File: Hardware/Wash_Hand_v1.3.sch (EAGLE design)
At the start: 62 parts, among them IC1 LM358D, IC2 LP298XS, IC3 405016TSSOP, J1 I2C, J2 ICSP, J3 SPI, J4 9V_CONN, J5 EXT_VCC, J6 6_PIN_SERIAL_CABLEPTH, Q1 16.0 Mhz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

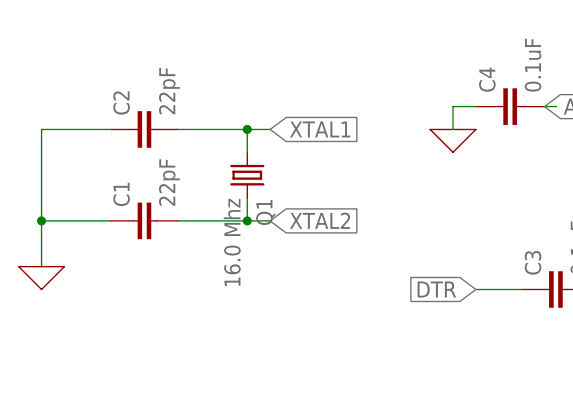
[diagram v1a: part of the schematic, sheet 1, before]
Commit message: Board/Schematic: Change 22pf to 10pf
Which makes the crystal work..

Signed-off-by: Konrad Rzeszutek Wilk <konrad@kernel.org>
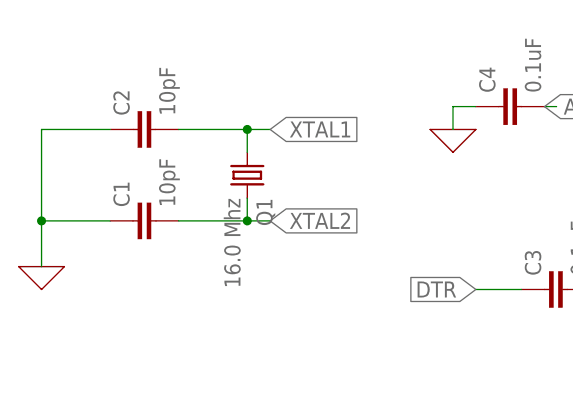
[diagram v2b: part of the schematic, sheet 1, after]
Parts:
- C1, C2: value 22pF -> 10pF
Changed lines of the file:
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@@
 <parts>
 <part name="Q1" library="adafruit" library_urn="urn:adsk.eagle:library:420" deviceset="CRYSTAL" device="HC49S" package3d_urn="urn:adsk.eagle:package:6240901/1" value="16.0 Mhz"/>
-<part name="C1" library="SparkFun-Capacitors" library_urn="urn:adsk.eagle:library:510" deviceset="10UF" device="-1206-6.3V-20%" package3d_urn="urn:adsk.eagle:package:37426/1" value="22pF"/>
-<part name="C2" library="SparkFun-Capacitors" library_urn="urn:adsk.eagle:library:510" deviceset="10UF" device="-1206-6.3V-20%" package3d_urn="urn:adsk.eagle:package:37426/1" value="22pF"/>
+<part name="C1" library="SparkFun-Capacitors" library_urn="urn:adsk.eagle:library:510" deviceset="10UF" device="-1206-6.3V-20%" package3d_urn="urn:adsk.eagle:package:37426/1" value="10pF"/>
+<part name="C2" library="SparkFun-Capacitors" library_urn="urn:adsk.eagle:library:510" deviceset="10UF" device="-1206-6.3V-20%" package3d_urn="urn:adsk.eagle:package:37426/1" value="10pF"/>
 <part name="X_2" library="ngspice-simulation" library_urn="urn:adsk.eagle:library:527439" deviceset="GND" device=""/>
 <part name="U$4" library="darnok_usb" deviceset="USB_MICROB_10118194_AMPHENOL" device="" package3d_urn="urn:adsk.eagle:package:21769933/1"/>

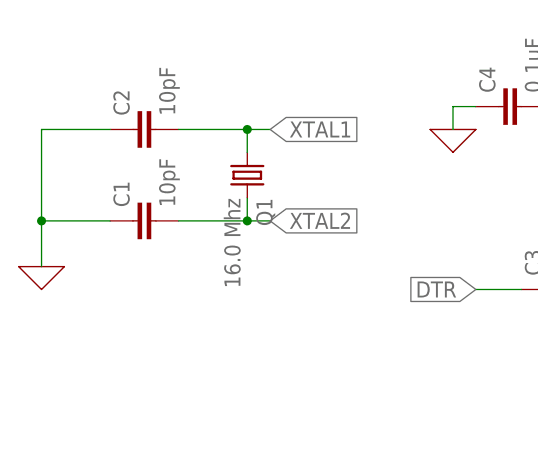
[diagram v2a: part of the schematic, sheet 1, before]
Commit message: Board/Schematic: Fix the 16MHz/10pF capacitors.
The way they are were in the schematic looked right.
Two capacitors off the crystal. Both capacitors go to
ground. Except that what Eagle decided it should be was:

XTAL1         XTAL2
|             |
+--[CRYSTAL]--+
             [CAP]
              |
             [CAP]
              |
             [GND]

Instead of the:

XTAL1         XTAL2
|             |
+--[CRYSTAL]--+
[CAP]        [CAP]
|             |
\------+------/
     [GND]

This fixes it.

Signed-off-by: Konrad Rzeszutek Wilk <konrad@kernel.org>
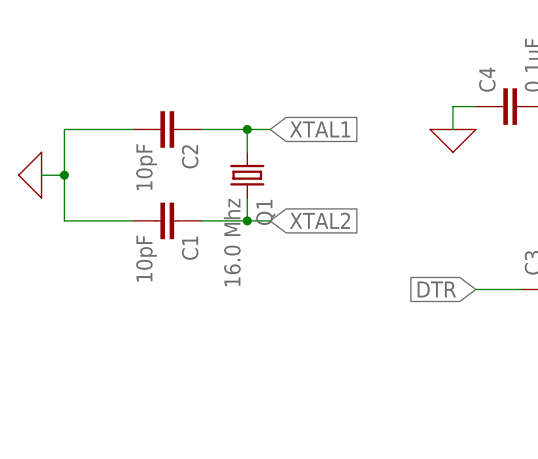
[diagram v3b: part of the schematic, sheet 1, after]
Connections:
- net 0: now also C1.2, C2.2; no longer C1.1, C2.1
- net XTAL1: now also C2.1; no longer C2.2
- net XTAL2: now also C1.1; no longer C1.2
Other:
- moved on the sheet: C1, C2
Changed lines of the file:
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@@
 <attribute name="VALUE" x="30.48" y="185.42" size="1.778" layer="96" rot="R270"/>
 </instance>
-<instance part="C1" gate="G$1" x="22.86" y="182.88" smashed="yes" rot="R90">
-<attribute name="NAME" x="19.939" y="184.404" size="1.778" layer="95" font="vector" rot="R90"/>
-<attribute name="VALUE" x="25.019" y="184.404" size="1.778" layer="96" font="vector" rot="R90"/>
-</instance>
-<instance part="C2" gate="G$1" x="22.86" y="193.04" smashed="yes" rot="R90">
-<attribute name="NAME" x="19.939" y="194.564" size="1.778" layer="95" font="vector" rot="R90"/>
-<attribute name="VALUE" x="25.019" y="194.564" size="1.778" layer="96" font="vector" rot="R90"/>
+<instance part="C1" gate="G$1" x="22.86" y="182.88" smashed="yes" rot="R270">
+<attribute name="NAME" x="25.781" y="181.356" size="1.778" layer="95" font="vector" rot="R270"/>
+<attribute name="VALUE" x="20.701" y="181.356" size="1.778" layer="96" font="vector" rot="R270"/>
+</instance>
+<instance part="C2" gate="G$1" x="22.86" y="193.04" smashed="yes" rot="R270">
+<attribute name="NAME" x="25.781" y="191.516" size="1.778" layer="95" font="vector" rot="R270"/>
+<attribute name="VALUE" x="20.701" y="191.516" size="1.778" layer="96" font="vector" rot="R270"/>
 </instance>
 <instance part="U$5" gate="G$1" x="210.82" y="76.2" smashed="yes">
@@
 <attribute name="VALUE" x="93.98" y="180.34" size="1.27" layer="96" rot="R90"/>
 </instance>
-<instance part="X_3" gate="G$1" x="10.16" y="177.8" smashed="yes"/>
+<instance part="X_3" gate="G$1" x="10.16" y="187.96" smashed="yes" rot="R270"/>
 <instance part="J1" gate="G$1" x="154.94" y="198.12" smashed="yes" rot="R180">
 <attribute name="VALUE" x="157.48" y="202.946" size="1.778" layer="96" font="vector" rot="R180"/>
@@
 <net name="0" class="0">
 <segment>
-<pinref part="X_3" gate="G$1" pin="0"/>
-<pinref part="C1" gate="G$1" pin="1"/>
-<wire x1="10.16" y1="193.04" x2="10.16" y2="182.88" width="0.1524" layer="91"/>
-<pinref part="C2" gate="G$1" pin="1"/>
-<wire x1="17.78" y1="193.04" x2="10.16" y2="193.04" width="0.1524" layer="91"/>
-<wire x1="17.78" y1="182.88" x2="10.16" y2="182.88" width="0.1524" layer="91"/>
-<junction x="10.16" y="182.88"/>
-<wire x1="10.16" y1="182.88" x2="10.16" y2="177.8" width="0.1524" layer="91"/>
-</segment>
-<segment>
 <pinref part="J5" gate="G$1" pin="1"/>
 <wire x1="38.1" y1="38.1" x2="45.72" y2="38.1" width="0.1524" layer="91"/>
@@
 <junction x="134.62" y="104.14"/>
 </segment>
+<segment>
+<pinref part="X_3" gate="G$1" pin="0"/>
+<wire x1="10.16" y1="187.96" x2="12.7" y2="187.96" width="0.1524" layer="91"/>
+<junction x="12.7" y="187.96"/>
+<wire x1="12.7" y1="187.96" x2="12.7" y2="193.04" width="0.1524" layer="91"/>
+<pinref part="C2" gate="G$1" pin="2"/>
+<wire x1="12.7" y1="193.04" x2="20.32" y2="193.04" width="0.1524" layer="91"/>
+<pinref part="C1" gate="G$1" pin="2"/>
+<wire x1="20.32" y1="182.88" x2="12.7" y2="182.88" width="0.1524" layer="91"/>
+<wire x1="12.7" y1="182.88" x2="12.7" y2="187.96" width="0.1524" layer="91"/>
+</segment>
 </net>
 <net name="D0" class="0">
@@
 <net name="XTAL2" class="0">
 <segment>
-<pinref part="C1" gate="G$1" pin="2"/>
 <pinref part="Q1" gate="G$1" pin="2"/>
-<wire x1="25.4" y1="182.88" x2="33.02" y2="182.88" width="0.1524" layer="91"/>
 <wire x1="33.02" y1="182.88" x2="33.02" y2="185.42" width="0.1524" layer="91"/>
 <wire x1="33.02" y1="182.88" x2="35.56" y2="182.88" width="0.1524" layer="91"/>
+<label x="35.56" y="182.88" size="1.778" layer="95" xref="yes"/>
+<pinref part="C1" gate="G$1" pin="1"/>
+<wire x1="27.94" y1="182.88" x2="33.02" y2="182.88" width="0.1524" layer="91"/>
 <junction x="33.02" y="182.88"/>
-<label x="35.56" y="182.88" size="1.778" layer="95" xref="yes"/>
 </segment>
 <segment>
@@
 <segment>
 <pinref part="Q1" gate="G$1" pin="1"/>
-<pinref part="C2" gate="G$1" pin="2"/>
-<wire x1="25.4" y1="193.04" x2="33.02" y2="193.04" width="0.1524" layer="91"/>
 <wire x1="33.02" y1="193.04" x2="33.02" y2="190.5" width="0.1524" layer="91"/>
 <wire x1="33.02" y1="193.04" x2="35.56" y2="193.04" width="0.1524" layer="91"/>
+<label x="35.56" y="193.04" size="1.778" layer="95" xref="yes"/>
 <junction x="33.02" y="193.04"/>
-<label x="35.56" y="193.04" size="1.778" layer="95" xref="yes"/>
-</segment>
-<segment>
+<pinref part="C2" gate="G$1" pin="1"/>
+<wire x1="33.02" y1="193.04" x2="27.94" y2="193.04" width="0.1524" layer="91"/>
+</segment>
+<segment>

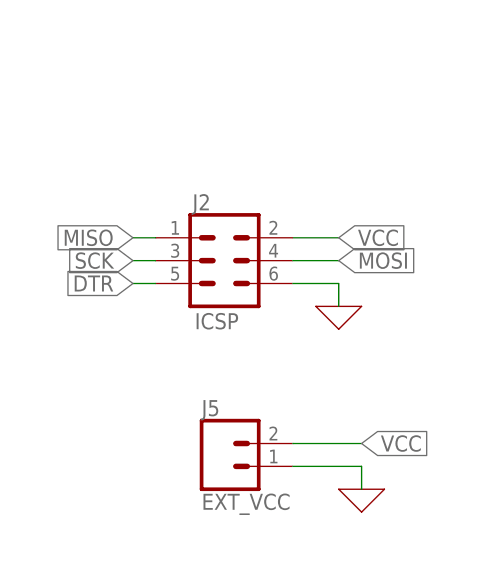
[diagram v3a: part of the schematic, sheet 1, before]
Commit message: Board/Schematic: Use RESET instead of DTR on ICSP
We don't want the line past the 0.1uF cap to go
in the ICSP but instead use the one that goes directly
to the RESET pin.

Signed-off-by: Konrad Rzeszutek Wilk <konrad@kernel.org>
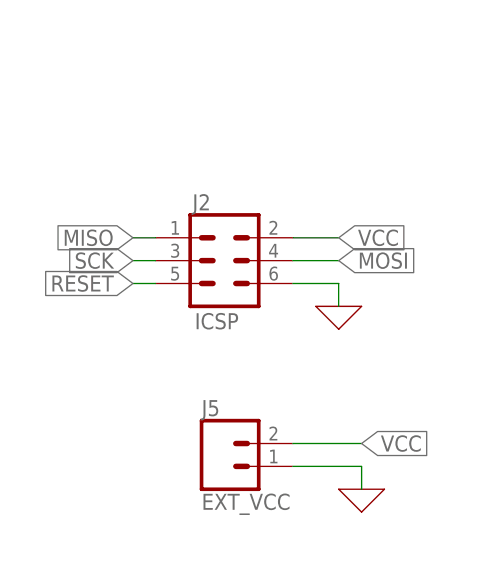
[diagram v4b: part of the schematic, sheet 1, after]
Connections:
- net DTR: no longer J2.5
- net RESET: now also J2.5
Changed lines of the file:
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@@
 <pinref part="U2" gate="U$1" pin="PC6(/RESET)"/>
+</segment>
+<segment>
+<pinref part="J2" gate="G$1" pin="5"/>
+<wire x1="22.86" y1="58.42" x2="20.32" y2="58.42" width="0.1524" layer="91"/>
+<label x="20.32" y="58.42" size="1.778" layer="95" rot="R180" xref="yes"/>
 </segment>
 </net>
@@
 </segment>
 <segment>
-<pinref part="J2" gate="G$1" pin="5"/>
-<wire x1="22.86" y1="58.42" x2="20.32" y2="58.42" width="0.1524" layer="91"/>
-<label x="20.32" y="58.42" size="1.778" layer="95" rot="R180" xref="yes"/>
-</segment>
-<segment>

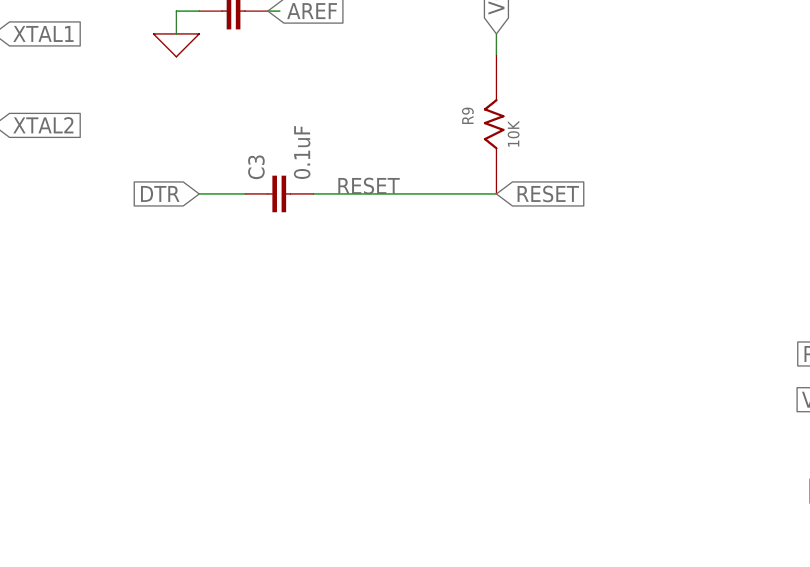
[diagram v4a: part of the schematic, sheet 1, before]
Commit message: Board/Schematic: Add 1K resistor to DTR line
As a pull-down resistor to smooth down the DTR.

Signed-off-by: Konrad Rzeszutek Wilk <konrad@kernel.org>
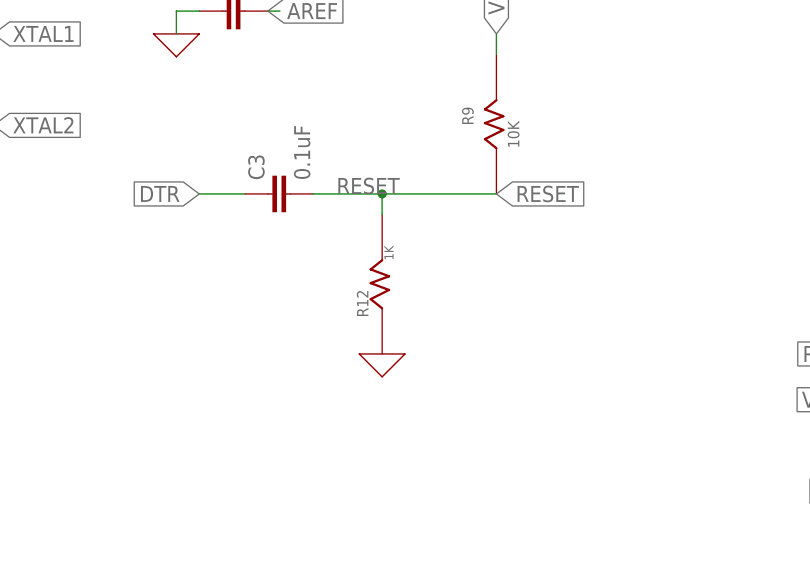
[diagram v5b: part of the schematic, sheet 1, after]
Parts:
- added R12: 1K, darnok_common:RESISTORR1206
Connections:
- net 0: now also R12.R_1
- net RESET: now also R12.R_2
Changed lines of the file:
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@@
 <part name="U2" library="SparkFun-IC-Microcontroller" library_urn="urn:adsk.eagle:library:525" deviceset="ATMEGA328P_TQFP" device="" package3d_urn="urn:adsk.eagle:package:38945/1" value="ATMEGA328P_TQFP"/>
 <part name="X_1" library="ngspice-simulation" library_urn="urn:adsk.eagle:library:527439" deviceset="GND" device=""/>
+<part name="X_28" library="ngspice-simulation" library_urn="urn:adsk.eagle:library:527439" deviceset="GND" device=""/>
+<part name="R12" library="darnok_common" deviceset="RESISTOR" device="R1206" value="1K"/>
 </parts>
 <sheets>
@@
 <attribute name="VALUE" x="142.24" y="93.98" size="1.778" layer="96"/>
 </instance>
+<instance part="X_28" gate="G$1" x="78.74" y="157.48" smashed="yes"/>
+<instance part="R12" gate="G$1" x="78.74" y="162.56" smashed="yes" rot="R90">
+<attribute name="NAME" x="77.216" y="161.544" size="1.27" layer="95" rot="R90"/>
+<attribute name="VALUE" x="80.01" y="167.894" size="1.016" layer="96" rot="R90"/>
+</instance>
 </instances>
 <busses>
@@
 <segment>
 <pinref part="R9" gate="G$1" pin="R_1"/>
-<wire x1="91.44" y1="175.26" x2="71.12" y2="175.26" width="0.1524" layer="91"/>
+<wire x1="91.44" y1="175.26" x2="78.74" y2="175.26" width="0.1524" layer="91"/>
 <label x="73.66" y="175.26" size="1.778" layer="95"/>
 <pinref part="C3" gate="G$1" pin="2"/>
 <label x="91.44" y="175.26" size="1.778" layer="95" xref="yes"/>
+<pinref part="R12" gate="G$1" pin="R_2"/>
+<wire x1="78.74" y1="175.26" x2="71.12" y2="175.26" width="0.1524" layer="91"/>
+<wire x1="78.74" y1="172.974" x2="78.74" y2="175.26" width="0.1524" layer="91"/>
+<junction x="78.74" y="175.26"/>
 </segment>
 <segment>
@@
 <wire x1="12.7" y1="182.88" x2="12.7" y2="187.96" width="0.1524" layer="91"/>
 </segment>
+<segment>
+<pinref part="X_28" gate="G$1" pin="0"/>
+<pinref part="R12" gate="G$1" pin="R_1"/>
+</segment>
 </net>

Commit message: Board/Schematic: Swap names (and values)of C6 and C7
They are right next to each other - and we want
the 1uF to be closer to MIC5205.

It was easier to swap the names than moving
the SMD on the board.

Signed-off-by: Konrad Rzeszutek Wilk <konrad@kernel.org>
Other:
- moved on the sheet: C6, C7
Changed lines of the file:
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@@
 <part name="MIC5205" library="SparkFun-IC-Power" library_urn="urn:adsk.eagle:library:526" deviceset="V_REG_MIC5205" device="5V" package3d_urn="urn:adsk.eagle:package:39060/1" value="5V"/>
 <part name="C5" library="SparkFun-Capacitors" library_urn="urn:adsk.eagle:library:510" deviceset="1.0UF" device="-1206-50V-10%" package3d_urn="urn:adsk.eagle:package:37426/1" value="1uF"/>
+<part name="C7" library="SparkFun-Capacitors" library_urn="urn:adsk.eagle:library:510" deviceset="1.0UF" device="-1206-50V-10%" package3d_urn="urn:adsk.eagle:package:37426/1" value="1uF"/>
 <part name="C6" library="SparkFun-Capacitors" library_urn="urn:adsk.eagle:library:510" deviceset="1.0UF" device="-1206-50V-10%" package3d_urn="urn:adsk.eagle:package:37426/1" value="2.2uF T"/>
-<part name="C7" library="SparkFun-Capacitors" library_urn="urn:adsk.eagle:library:510" deviceset="1.0UF" device="-1206-50V-10%" package3d_urn="urn:adsk.eagle:package:37426/1" value="1uF"/>
 <part name="X_9" library="ngspice-simulation" library_urn="urn:adsk.eagle:library:527439" deviceset="GND" device=""/>
 <part name="X_10" library="ngspice-simulation" library_urn="urn:adsk.eagle:library:527439" deviceset="GND" device=""/>
@@
 <attribute name="VALUE" x="143.764" y="91.821" size="1.778" layer="96" font="vector"/>
 </instance>
-<instance part="C6" gate="G$1" x="177.8" y="96.52" smashed="yes">
+<instance part="C7" gate="G$1" x="177.8" y="96.52" smashed="yes">
 <attribute name="NAME" x="179.324" y="99.441" size="1.778" layer="95" font="vector"/>
 <attribute name="VALUE" x="179.324" y="94.361" size="1.778" layer="96" font="vector"/>
 </instance>
-<instance part="C7" gate="G$1" x="187.96" y="96.52" smashed="yes">
+<instance part="C6" gate="G$1" x="187.96" y="96.52" smashed="yes">
 <attribute name="NAME" x="189.484" y="99.441" size="1.778" layer="95" font="vector"/>
 <attribute name="VALUE" x="189.484" y="94.361" size="1.778" layer="96" font="vector"/>
@@
 <segment>
 <pinref part="X_11" gate="G$1" pin="0"/>
+<pinref part="C7" gate="G$1" pin="2"/>
+<wire x1="177.8" y1="88.9" x2="177.8" y2="93.98" width="0.1524" layer="91"/>
+</segment>
+<segment>
+<pinref part="X_12" gate="G$1" pin="0"/>
 <pinref part="C6" gate="G$1" pin="2"/>
-<wire x1="177.8" y1="88.9" x2="177.8" y2="93.98" width="0.1524" layer="91"/>
-</segment>
-<segment>
-<pinref part="X_12" gate="G$1" pin="0"/>
-<pinref part="C7" gate="G$1" pin="2"/>
 <wire x1="187.96" y1="88.9" x2="187.96" y2="93.98" width="0.1524" layer="91"/>
 </segment>
@@
 <segment>
 <pinref part="MIC5205" gate="U1" pin="OUT"/>
+<pinref part="C7" gate="G$1" pin="1"/>
+<wire x1="170.18" y1="101.6" x2="177.8" y2="101.6" width="0.1524" layer="91"/>
 <pinref part="C6" gate="G$1" pin="1"/>
-<wire x1="170.18" y1="101.6" x2="177.8" y2="101.6" width="0.1524" layer="91"/>
-<pinref part="C7" gate="G$1" pin="1"/>
 <wire x1="187.96" y1="101.6" x2="177.8" y2="101.6" width="0.1524" layer="91"/>
 <junction x="177.8" y="101.6"/>
